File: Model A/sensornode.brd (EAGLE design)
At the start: 50 x 50 mm, 42 parts, among them U1 ATMEGA328P_PDIP

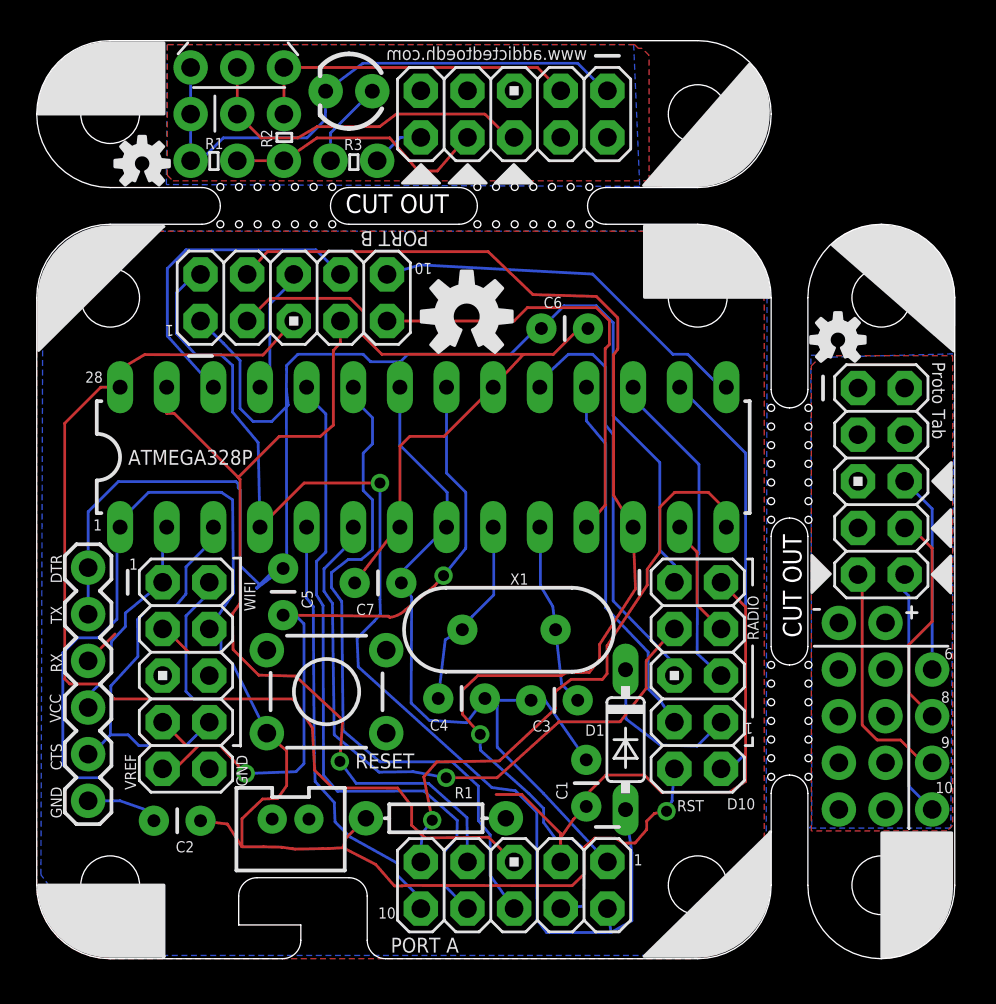
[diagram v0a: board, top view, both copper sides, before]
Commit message: fixed sensornode radio direction, power pin labels
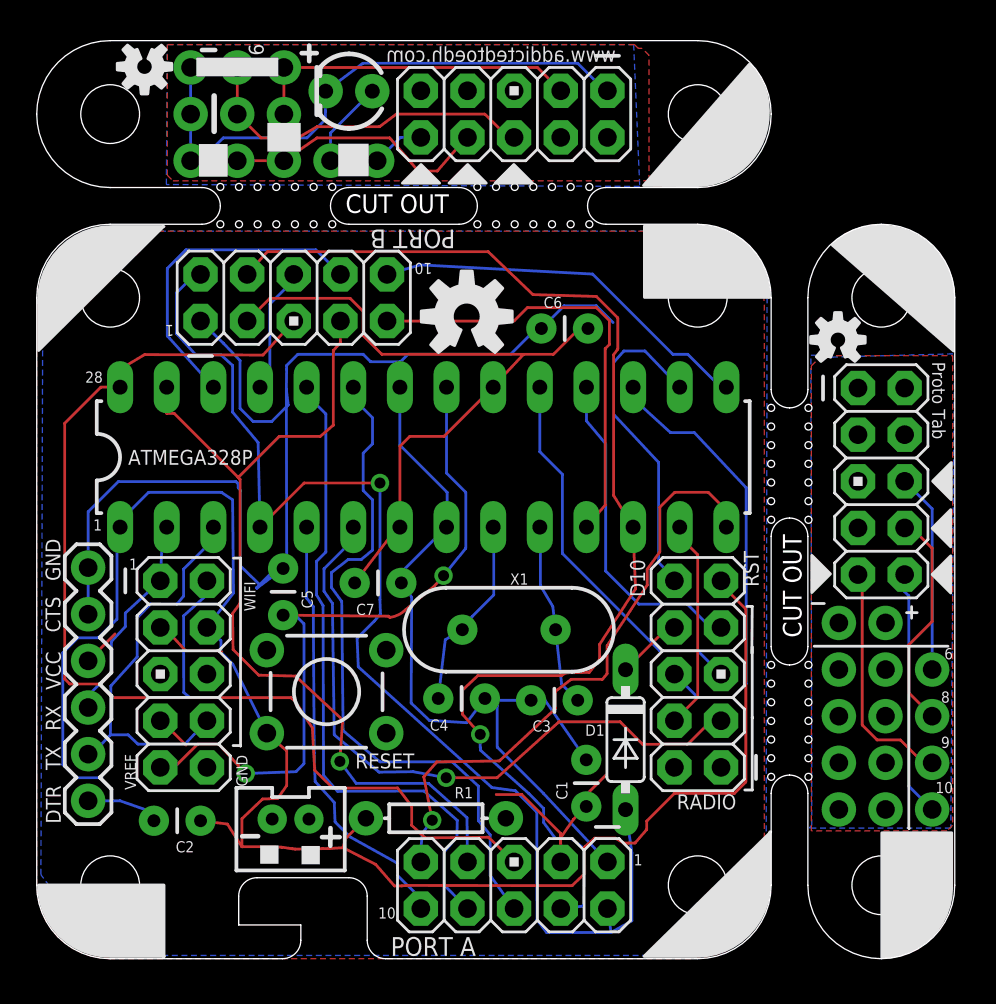
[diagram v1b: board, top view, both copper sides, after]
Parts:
- moved U$7 5.28 mm to (5.87, 48.6), turned to 180 degrees
- moved JP8 0.15 mm to (8.00, 15.5)
- moved RF24 0.08 mm to (36.0, 15.5), turned to 180 degrees
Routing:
- net VCC: track 77.8 -> 58.5 mm
- net GND: track 134.2 -> 119.2 mm
- net N$2: track 81.1 -> 95.3 mm, vias 1 -> 0
- net N$16: track 17.8 -> 24.2 mm
- net N$24: track 8.88 -> 3.61 mm
- net N$4: track 23.1 -> 17.9 mm
- net N$20: track 6.48 -> 11.5 mm
- net N$23: track 23.1 -> 20.9 mm
- net N$26: track 20.1 -> 17.9 mm
